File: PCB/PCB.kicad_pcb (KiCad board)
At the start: 2 copper layers, 115 x 77 mm, 153 parts, among them J1 Conn_01x06, J2 Screw_Terminal_01x04, J3 Screw_Terminal_01x08, J4 Conn_02x06_Odd_Even, J5 Conn_01x03, U1 ESP32-S3, U10 TPS22918DBV, U2 PC817, U3 PC817, U4 ADuM1411, U5 ATM90E36A-AU-R, U6 HLK-5M05, U7 B0303S-1WR3, U8 BQ24073RGT, U9 TLV75733PDRV, Y1 ABM8W-16.3840MHZ-4-B1U-T3

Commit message: edited the PCB layout
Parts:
- added D8: LED_L3, LED_SMD:LED_0603_1608Metric, F.Cu at (89.8, 126.1)
- added J10: Conn_01x02, Connector_PinHeader_2.54mm:PinHeader_1x02_P2.54mm_Vertical, F.Cu at (92.4, 124.9)
- added J6: Conn_01x04, Connector_PinHeader_2.54mm:PinHeader_1x04_P2.54mm_Vertical, F.Cu at (115.5, 81.6)
- added J7: Conn_01x02, Connector_PinHeader_2.54mm:PinHeader_1x02_P2.54mm_Vertical, F.Cu at (107.9, 124.8)
- added J8: Conn_01x02, Connector_PinHeader_2.54mm:PinHeader_1x02_P2.54mm_Vertical, F.Cu at (102.7, 124.9)
- added J9: Conn_01x02, Connector_PinHeader_2.54mm:PinHeader_1x02_P2.54mm_Vertical, F.Cu at (97.5, 124.9)
- added R68: 10k, Resistor_SMD:R_0603_1608Metric, F.Cu at (112.8, 85.8)
- added R69: 10k, Resistor_SMD:R_0603_1608Metric, F.Cu at (112.8, 90.0)
- added R70: 1k, Resistor_SMD:R_0603_1608Metric, F.Cu at (89.8, 123.0)
- added TP12: TestPoint, TestPoint:TestPoint_Pad_D1.0mm, F.Cu at (144.0, 98.6)
- added TP14: TestPoint, TestPoint:TestPoint_Pad_D1.0mm, F.Cu at (139.9, 101.1)
- added TP28: TestPoint, TestPoint:TestPoint_Pad_D1.0mm, F.Cu at (129.6, 100.7)
- moved J1 43.8 mm to (94.7, 134.8)
- moved J4 41.0 mm to (127.9, 136.3), turned to 90 degrees
- moved TP23 39.3 mm to (109.5, 81.2), turned to -90 degrees
- moved C35 37.0 mm to (104.3, 88.0), turned to 0 degrees
- moved C31 35.9 mm to (108.4, 83.1), turned to 180 degrees
- moved C33 35.9 mm to (107.6, 80.8), turned to -90 degrees
- moved U10 35.8 mm to (99.0, 92.8)
- moved C36 35.8 mm to (96.1, 92.7)
- moved TP22 35.4 mm to (102.0, 90.2)
- moved C34 35.4 mm to (104.3, 86.5), turned to 0 degrees
- moved U9 34.6 mm to (109.8, 85.3), turned to 90 degrees
- moved C32 34.0 mm to (106.0, 80.8), turned to -90 degrees
- moved R63 33.2 mm to (98.7, 88.5), turned to 180 degrees
- moved R60 33.1 mm to (94.2, 95.0), turned to -90 degrees
- moved TP20 32.7 mm to (94.0, 92.2)
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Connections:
- net /Digital/EN renamed /EN
- net /Digital/IO0 renamed /IO0
- net /Digital/IO14 renamed /IO14
- net /Digital/IO17 renamed /IO17
- net /Digital/IO18 renamed /IO18
- net /Digital/IO21 renamed /IO21
- net /Digital/IO3 renamed /IO3
- net /Digital/IO35 renamed /IO35
- net /Digital/IO36 renamed /IO36
- net /Digital/IO37 renamed /IO37
- net /Digital/IO38 renamed /IO38
- net /Digital/IO39 renamed /IO39
- net /Digital/IO4 renamed /IO4
- net /Digital/IO42 renamed /IO42
- net /Digital/IO46 renamed /IO46
- net /Digital/IO47 renamed /IO47
- net /Digital/IO8 renamed /IO8
- net /Digital/IO9 renamed /IO9
- net /Digital/LED_L1 renamed /LED_L1
- net /Digital/LED_L2 renamed /LED_L2
- net /Digital/LED_L3 renamed /LED_L3
- net /Digital/MCU_CS renamed /MCU_CS
- net /Digital/MCU_MISO renamed /MCU_MISO
- net /Digital/MCU_MOSI renamed /MCU_MOSI
- net /Digital/MCU_SCLK renamed /MCU_SCLK
- net /Digital/RXD0 renamed /RXD0
- net /Digital/TXD0 renamed /TXD0
- net /Digital/USB_D+ renamed /USB_D+
- net /Digital/USB_D- renamed /USB_D-
- net /Energy Metering/I1N renamed /I1N
- net /Energy Metering/I1P renamed /I1P
- net /Energy Metering/I2N renamed /I2N
- net /Energy Metering/I2P renamed /I2P
- net /Energy Metering/I3N renamed /I3N
- net /Energy Metering/I3P renamed /I3P
- net /Energy Metering/I4N renamed /I4N
- net /Energy Metering/I4P renamed /I4P
- net /Energy Metering/OSCI renamed /OSCI
- net /Energy Metering/OSCO renamed /OSCO
- net /Energy Metering/V1N renamed /V1N
- net /Energy Metering/V1P renamed /V1P
- net /Energy Metering/V2N renamed /V2N
- net /Energy Metering/V2P renamed /V2P
- net /Energy Metering/V3N renamed /V3N
- net /Energy Metering/V3P renamed /V3P
- net /Energy Metering/VREF renamed /VREF
- net /Supply/CHG renamed /CHG
- net /Supply/ILIM renamed /ILIM
- net /Supply/ISET renamed /ISET
- net /Supply/PG renamed /PG
- net /Supply/TD renamed /TD
- net /Supply/TMR renamed /TMR
- net /Supply/TS renamed /TS
- J4 pad 1: /Energy Metering/CF4 -> /IRQ0
- J4 pad 10: /Energy Metering/CF2 -> /ZX2
- J4 pad 12: /Energy Metering/CF3 -> /ZX0
- J4 pad 2: /Energy Metering/ZX0 -> /DMA
- J4 pad 3: /Energy Metering/WARN -> /CF2
- J4 pad 4: /Energy Metering/ZX1 -> /CF4
- J4 pad 5: /Energy Metering/IRQ0 -> /IRQ1
- J4 pad 6: /Energy Metering/ZX2 -> /CF1
- J4 pad 7: /Energy Metering/IRQ1 -> /CF3
- J4 pad 8: /Energy Metering/CF1 -> /WARN
- J4 pad 9: /Energy Metering/DMA -> /ZX1
- U1 pad 25: /Digital/IO48 -> /PMC_1
- U1 pad 26: /Digital/IO45 -> /PMC_0
- U1 pad 33: /Digital/IO40 -> /SDA
- U1 pad 34: /Digital/IO41 -> /SCL
- U1 pad 5: /Digital/PMC_0 -> /IO5
- U1 pad 6: /Digital/PMC_1 -> /LED_WIFI
- U2 pad 2: /Digital/PMC_0 -> /PMC_0
- U3 pad 2: /Digital/PMC_1 -> /PMC_1
- U5 pad 22: /Energy Metering/ZX0 -> /ZX0
- U5 pad 23: /Energy Metering/ZX1 -> /ZX1
- U5 pad 24: /Energy Metering/ZX2 -> /ZX2
- U5 pad 25: /Energy Metering/CF1 -> /CF1
- U5 pad 26: /Energy Metering/CF2 -> /CF2
- U5 pad 27: /Energy Metering/CF3 -> /CF3
- U5 pad 28: /Energy Metering/CF4 -> /CF4
- U5 pad 29: /Energy Metering/WARN -> /WARN
- U5 pad 30: /Energy Metering/IRQ0 -> /IRQ0
- U5 pad 31: /Energy Metering/IRQ1 -> /IRQ1
- U5 pad 36: /Energy Metering/DMA -> /DMA
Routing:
- net +3V3PWR: track 114.7 -> 0.00 mm, vias 6 -> 0
- net +3V3: track 112.8 -> 0.00 mm, vias 5 -> 0
- net L1: track 43.3 -> 0.00 mm
- net /Digital/PMC_0: track 36.0 -> 0.00 mm, vias 2 -> 0
- net +VBAT_IN: track 34.6 -> 0.00 mm, vias 2 -> 0
- net /EN: track 30.6 -> 0.00 mm
- net /Digital/PMC_1: track 30.3 -> 0.00 mm, vias 2 -> 0
- net MISO: track 32.3 -> 2.28 mm
- net MOSI: track 31.8 -> 1.99 mm
- net PM0: track 29.3 -> 0.00 mm
- net BAT_SW: track 28.4 -> 0.00 mm, vias 2 -> 0
- net PM1: track 27.2 -> 0.00 mm
- net +VIN: track 26.4 -> 0.00 mm, vias 2 -> 0
- net ~{CS}: track 26.4 -> 0.00 mm
- net SCLK: track 28.1 -> 1.69 mm
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- removed copper zone on F.Cu, net +3V3PWR
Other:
- board size 115 x 77 mm -> 78 x 90 mm

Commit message: PCB routing and adjusts
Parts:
- added TP21: TestPoint, TestPoint:TestPoint_Pad_D1.5mm, F.Cu at (105.6, 94.8)
- moved D8 2.45 mm to (91.9, 78.4)
- moved R66 2.45 mm to (88.8, 78.4)
- moved D7 2.17 mm to (91.9, 80.6)
- moved R65 2.13 mm to (88.8, 80.6)
- moved TP13 0.21 mm to (141.5, 109.3)
- moved TP17 0.16 mm to (109.6, 81.1)
- moved C5 0.13 mm to (124.8, 120.1)
- renumbered C26 to C18, C39 to C19, C18 to C20, C19 to C21, C20 to C22, C21 to C23, C22 to C24, C23 to C25, C24 to C26, C37 to C27, C38 to C28, C25 to C29, C27 to C30, C28 to C31, C29 to C32, C30 to C33, C31 to C34, C32 to C35, C33 to C36, C34 to C37, C35 to C38, C36 to C39, D8 to D4, D4 to D5, D5 to D6, D6 to D7, D7 to D8, J9 to J1, J5 to J10, J8 to J2, J6 to J3, J1 to J4, J7 to J5, J10 to J6, J2 to J7, J3 to J8, J4 to J9, JP2 to JP1, R7 to R10, R8 to R11, R9 to R12, R10 to R13, R11 to R14, R12 to R15, R13 to R16, R14 to R17, R15 to R18, R16 to R19, R17 to R20, R18 to R21, R19 to R22, R20 to R23, R21 to R24, R22 to R25, R23 to R26, R30 to R27, R31 to R28, R35 to R29, R36 to R30, R24 to R31, R25 to R32, R26 to R33, R27 to R34, R28 to R35, R29 to R36, R32 to R37, R33 to R38, R34 to R39, R68 to R4, R37 to R40, R38 to R41, R39 to R42, R40 to R43, R41 to R44, R42 to R45, R44 to R46, R45 to R47, R47 to R48, R48 to R49, R69 to R5, R43 to R50, R46 to R51, R64 to R52, R65 to R53, R49 to R54, R66 to R55, R67 to R56, R50 to R57, R51 to R58, R52 to R59, R70 to R6, R53 to R60, R54 to R61, R55 to R62, R56 to R63, R57 to R64, R58 to R65, R59 to R66, R60 to R67, R61 to R68, R62 to R69, R4 to R7, R63 to R70, R5 to R8, R6 to R9, TP7 to TP1, TP28 to TP10, TP25 to TP11, TP26 to TP12, TP17 to TP13, TP18 to TP14, TP19 to TP15, TP24 to TP16, TP23 to TP17, TP22 to TP18, TP20 to TP19, TP8 to TP2, TP21 to TP20, TP9 to TP3, TP10 to TP4, TP11 to TP5, TP15 to TP6, TP16 to TP7, TP12 to TP8, TP14 to TP9
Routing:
- net +3V3: track 0.00 -> 153.9 mm, vias 0 -> 2
- net +3V3PWR: track 0.00 -> 70.8 mm, vias 0 -> 5
- net +VIN: track 0.00 -> 49.0 mm, vias 0 -> 3
- net /IO0: track 0.00 -> 42.8 mm
- net +5V_EXT: track 0.00 -> 41.2 mm
- net /RXD0: track 0.00 -> 40.3 mm
- net /TXD0: track 0.00 -> 39.8 mm
- net L1: track 0.00 -> 32.6 mm
- net /ZX1: track 0.00 -> 27.6 mm
- net /SCL: track 0.00 -> 26.2 mm
- net /CF2: track 0.00 -> 25.7 mm
- net /CF3: track 0.00 -> 25.5 mm
- net /ZX0: track 0.00 -> 24.9 mm
- net /EN: track 0.00 -> 24.4 mm
- net /ZX2: track 0.00 -> 24.2 mm
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- added copper zone on F.Cu, net +3V3PWR
- added copper zone on B.Cu, net GND
- added copper zone on F.Cu, net GND
- added copper zone on B.Cu, net N
- added copper zone on F.Cu, net N
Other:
- board text added: "+3V3"
- board text added: "+5V"
- board text added: "+VBAT"
- board text added: "+VBAT_IN"
- board text added: "+VIN"
- board text added: "3V3"
- board text added: "3V3PWR"
- board text added: "ADC_BAT"
- board text added: "ALTERAR EXPANSÃO DA MASCARA DE SOLDA DO U5"
- board text added: "EN"
- board text added: "GND"
- board text added: "I1+"
- board text added: "I1-"
- board text added: "I2+"
- board text added: "I2-"
- board text added: "I3+"
- board text added: "I3-"
- board text added: "IN+"
- board text added: "IN-"
- board text added: "IO0"
- board text added: "NEUTRAL"
- board text added: "OLED I2C"
- board text added: "RX"
- board text added: "SCL"
- board text added: "SDA"
- board text added: "TTL"
- board text added: "TX"
- board text added: "V1P"
- board text added: "V2P"
- board text added: "V3P"
- board text added: "VREF"

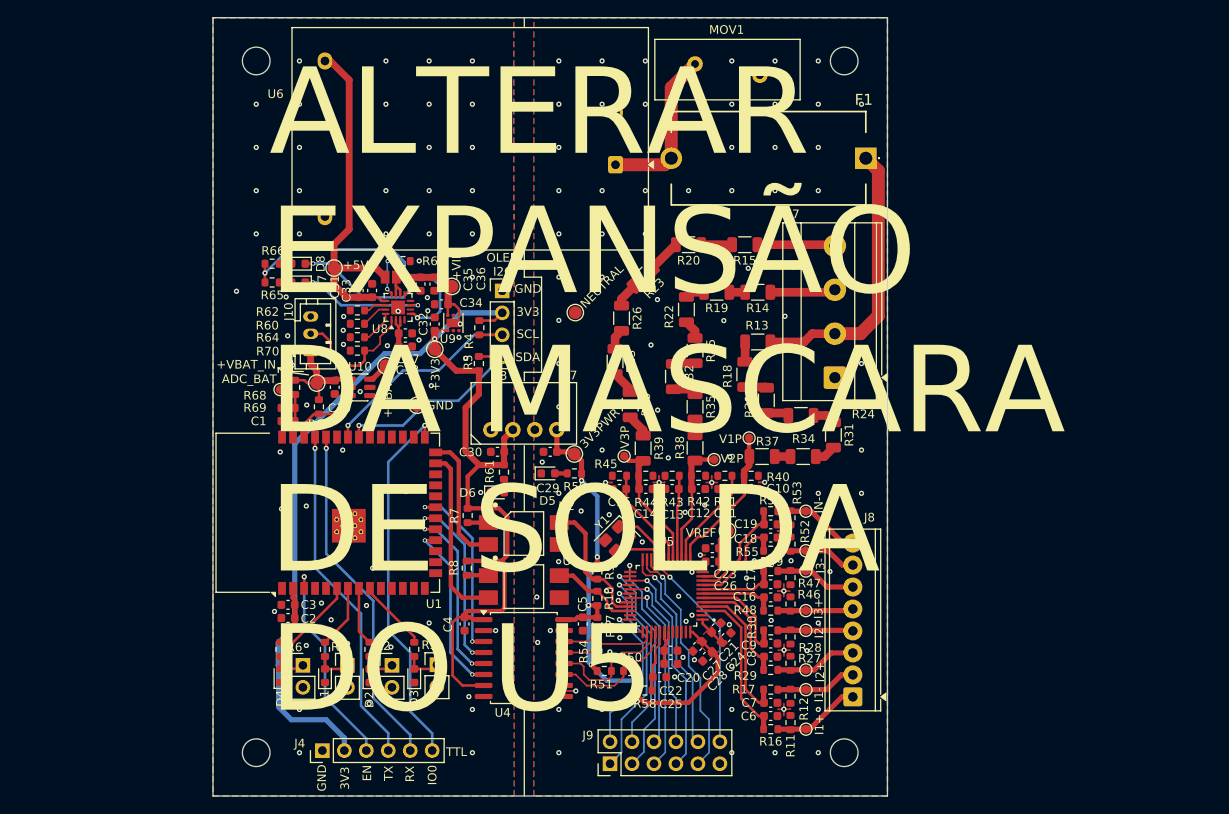
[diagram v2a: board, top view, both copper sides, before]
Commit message: altered the solder mask expansion and added pcb cutout under esp antenna
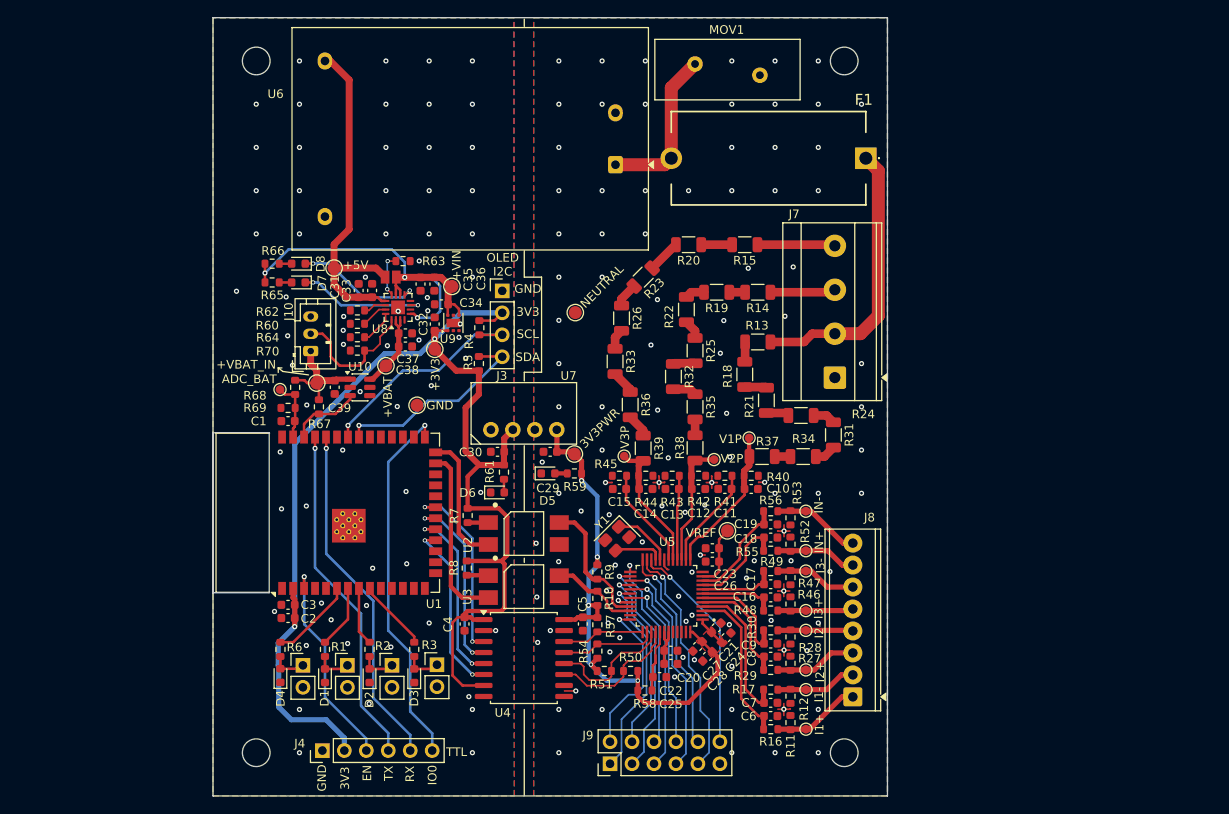
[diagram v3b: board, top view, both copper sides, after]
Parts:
- U2, U3: footprint 1lib:SOIC-4_6.5x4.6_P2.54mm -> myLIB:SOIC-4_6.5x4.6_P2.54mm
- U5: footprint 1lib:48TQFP -> myLIB:48TQFP
- U7: footprint 1lib:B0303S-1WR3 -> myLIB:B0303S-1WR3
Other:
- outline, holes or cut-outs redrawn
- board text removed: "ALTERAR EXPANSÃO DA MASCARA DE SOLDA DO U5"

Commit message: added cutout for esp antenna
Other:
- outline, holes or cut-outs redrawn
- board text added: "1"
- board text added: "2"
- board text added: "3"
- board text added: "4"
- board text added: "5"
- board text added: "6"
- board text added: "7"
- board text added: "8"
- board text added: "9"

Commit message: finished layout, added gerber files, added BOM
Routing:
- net GND: track 0.00 -> 3.46 mm, vias 69 -> 99
- net MOSI: track 15.3 -> 14.7 mm
- net N: vias 104 -> 131

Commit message: new readme, added .step models to pcb
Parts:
- F1: footprint 1lib:FuseHolder_5x20mm_P=22,5mm -> myLIB:FuseHolder_5x20mm_P=22,5mm

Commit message: added pullup resistor on EN pin + cap to gnd on the same pin
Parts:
- added C40: 100n/16V, Capacitor_SMD:C_0603_1608Metric, F.Cu at (93.9, 117.9)
- added R71: 10k, Resistor_SMD:R_0603_1608Metric, F.Cu at (93.2, 120.2)
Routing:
- net +3V3: track 153.9 -> 155.9 mm
- net /EN: track 24.4 -> 22.9 mm
- net /LED_WIFI: track 9.80 -> 11.2 mm
- net GND: vias 99 -> 97
